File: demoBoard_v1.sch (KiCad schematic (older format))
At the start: 47 parts, among them P1 SPI_Header, P10 RTC_Serial, P11 WD_Header, P12 WD_1.2V_NC, P13 RTC_Aux, P14 Flash_3v3_NC, P15 WD_SENSE_3.3V_NC, P2 3x_CS_Header, P3 Power_Header, P4 LOAD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

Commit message: Fixed SEL monitor mistake ground connection
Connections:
- wire segments 172 -> 170
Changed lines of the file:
@@
 Text GLabel 4150 4800 2    60   Input ~ 0
 Load+
-Text GLabel 1250 3500 3    60   Input ~ 0
-INA_GND
 $Comp
 L DMN2075U Q1
@@
 Wire Wire Line
 	1000 7100 1000 7200
-Connection ~ 1100 3450
-Wire Wire Line
-	1250 3450 1100 3450
-Wire Wire Line
-	1250 3500 1250 3450
 Wire Wire Line
 	950  3400 900  3400
@@
 	1900 1100 1750 1100
 Wire Wire Line
-	9400 1100 9100 1100
+	9100 1100 9400 1100
 Wire Wire Line
 	9250 1100 9250 850

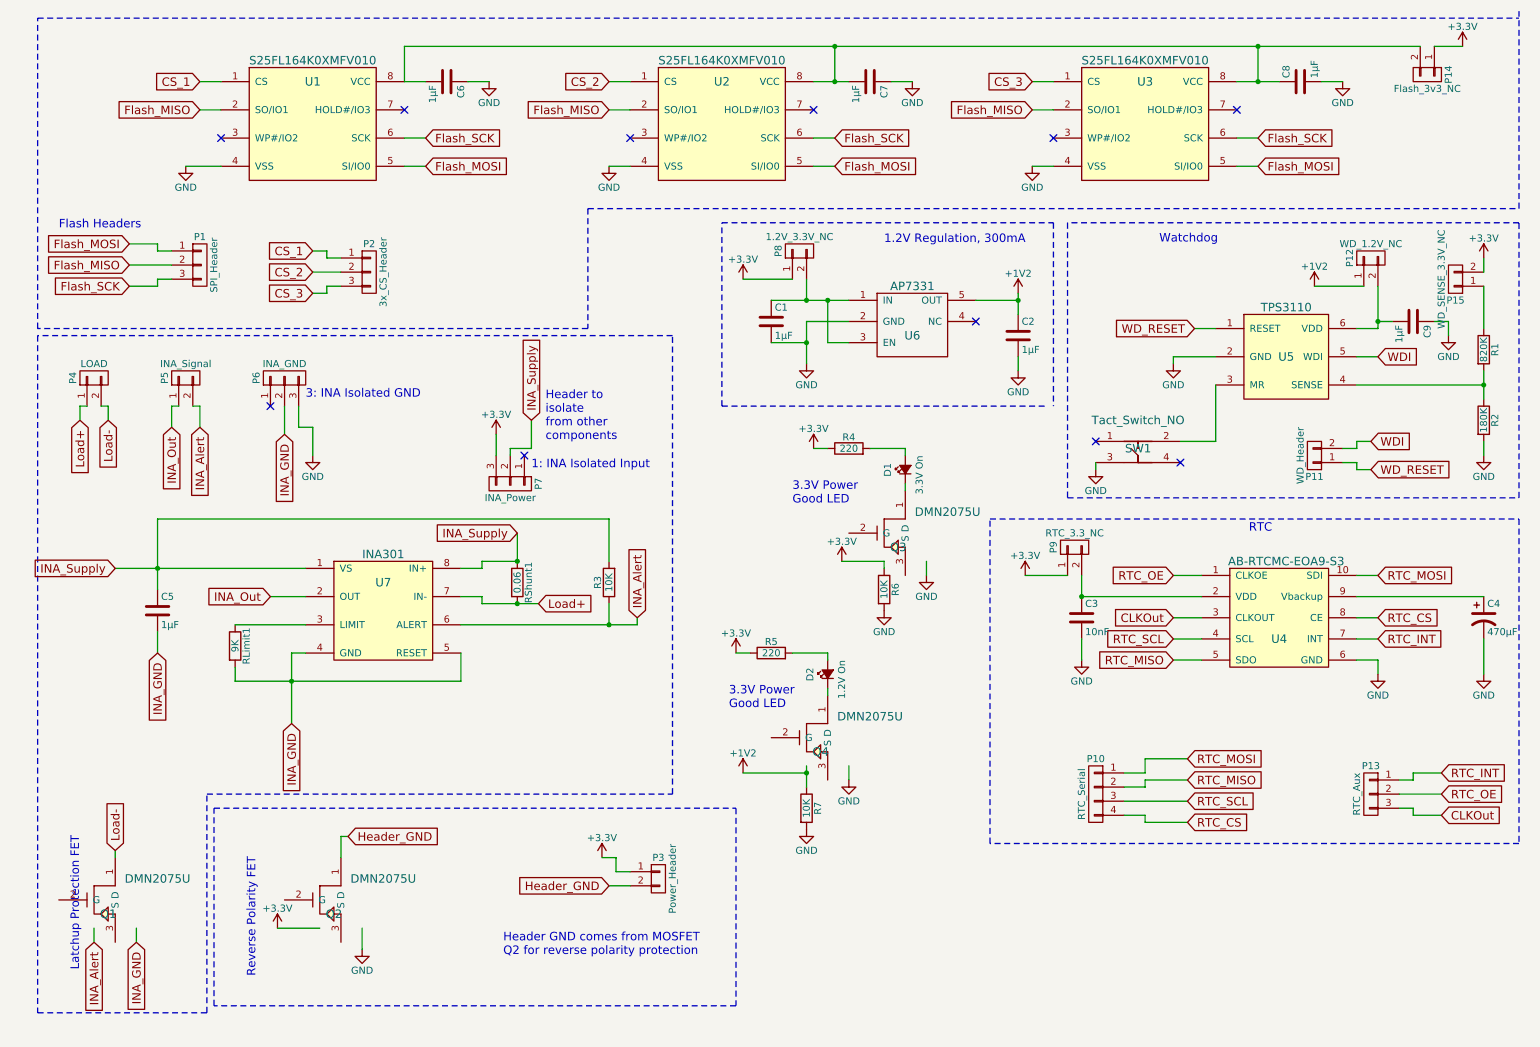
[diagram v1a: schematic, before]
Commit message: Added TVS and INA indicator LED to schematic. Committing before adding footprint and PCB traces.
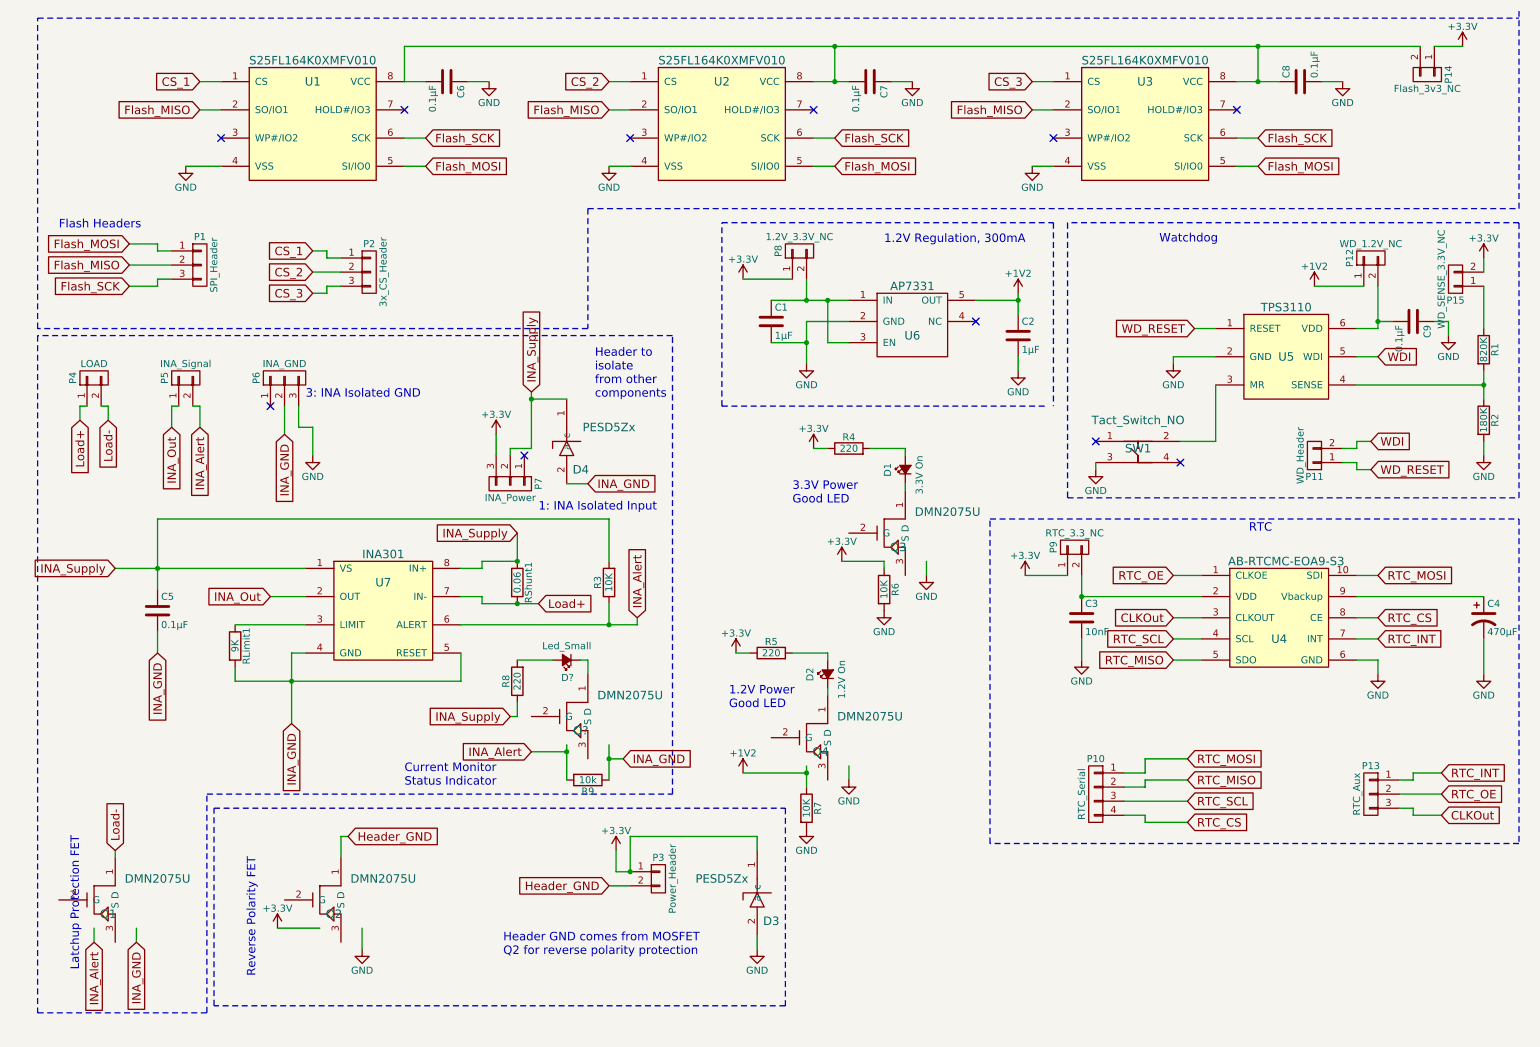
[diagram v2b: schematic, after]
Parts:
- added D3, D4: PESD5Zx, symbol PESD5Zx
- added D?: Led_Small, symbol Led_Small
- added Q?: DMN2075U, symbol DMN2075U
- added R8: 220, symbol R
- added R9: 10k, symbol R
- C5, C6, C7, C8, C9: value 1µF -> 0.1µF
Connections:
- wire segments 170 -> 184
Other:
- note added: "1.2V Power \nGood LED"
- note added: "Current Monitor\nStatus Indicator"

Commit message: Ready to be sent to board house
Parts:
- added R10: 0, Resistors_SMD:R_0402, symbol R
- D3, D4: footprint (none) -> SFUSat:PESD57zx
- D5: renamed from D?; footprint (none) -> SFUSat:LED_150060GS75000
- Q5: renamed from Q?; footprint (none) -> SFUSat:SOT23_DMN2075U
- R8, R9: footprint (none) -> Resistors_SMD:R_0402
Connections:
- wire segments 184 -> 185
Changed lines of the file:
@@
 F 0 "D3" H 5800 6650 60  0000 C CNN
 F 1 "PESD5Zx" H 5450 6950 60  0000 C CNN
-F 2 "" H 5700 6850 60  0001 C CNN
+F 2 "SFUSat:PESD57zx" H 5700 6850 60  0001 C CNN
 F 3 "" H 5700 6850 60  0001 C CNN
 	1    5700 6850
@@
 $EndComp
 $Comp
-L GND #PWR?
+L GND #PWR035
 U 1 1 5924F4C6
 P 5700 7250
-F 0 "#PWR?" H 5700 7000 50  0001 C CNN
+F 0 "#PWR035" H 5700 7000 50  0001 C CNN
 F 1 "GND" H 5700 7100 50  0000 C CNN
 F 2 "" H 5700 7250 50  0000 C CNN
@@
 F 0 "D4" H 4450 3450 60  0000 C CNN
 F 1 "PESD5Zx" H 4650 3750 60  0000 C CNN
-F 2 "" H 4350 3650 60  0001 C CNN
+F 2 "SFUSat:PESD57zx" H 4350 3650 60  0001 C CNN
 F 3 "" H 4350 3650 60  0001 C CNN
 	1    4350 3650
@@
 INA_GND
 $Comp
-L DMN2075U Q?
+L DMN2075U Q5
 U 1 1 592523F8
 P 4500 5600
-F 0 "Q?" H 4450 5500 60  0000 C CNN
+F 0 "Q5" H 4450 5500 60  0000 C CNN
 F 1 "DMN2075U" H 4800 5750 60  0000 C CNN
-F 2 "" H 4450 5500 60  0001 C CNN
+F 2 "SFUSat:SOT23_DMN2075U" H 4450 5500 60  0001 C CNN
 F 3 "" H 4450 5500 60  0001 C CNN
 	1    4500 5600
@@
 $EndComp
 $Comp
-L Led_Small D?
+L Led_Small D5
 U 1 1 59252552
 P 4350 5200
-F 0 "D?" H 4300 5325 50  0000 L CNN
+F 0 "D5" H 4300 5325 50  0000 L CNN
 F 1 "Led_Small" H 4175 5100 50  0000 L CNN
-F 2 "" V 4350 5200 50  0000 C CNN
+F 2 "SFUSat:LED_150060GS75000" V 4350 5200 50  0001 C CNN
 F 3 "" V 4350 5200 50  0000 C CNN
 	1    4350 5200
@@
 F 0 "R8" V 4080 5350 50  0000 C CNN
 F 1 "220" V 4000 5350 50  0000 C CNN
-F 2 "" V 3930 5350 50  0000 C CNN
+F 2 "Resistors_SMD:R_0402" V 3930 5350 50  0001 C CNN
 F 3 "" H 4000 5350 50  0000 C CNN
 	1    4000 5350
@@
 F 0 "R9" V 4580 6050 50  0000 C CNN
 F 1 "10k" V 4500 6050 50  0000 C CNN
-F 2 "" V 4430 6050 50  0000 C CNN
+F 2 "Resistors_SMD:R_0402" V 4430 6050 50  0001 C CNN
 F 3 "" H 4500 6050 50  0000 C CNN
 	1    4500 6050
@@
 	4350 5850 4100 5850
 Connection ~ 4350 5850
-Text GLabel 3950 5600 0    60   Input ~ 0
+Text GLabel 3450 5600 0    60   Input ~ 0
 INA_Supply
 Wire Wire Line
-	3950 5600 4000 5600
+	3850 5600 4000 5600
 Wire Wire Line
 	4000 5600 4000 5500
 Text Notes 3200 6100 0    60   ~ 0
 Current Monitor\nStatus Indicator
+$Comp
+L R R10
+U 1 1 5925159D
+P 3700 5600
+F 0 "R10" V 3780 5600 50  0000 C CNN
+F 1 "0" V 3700 5600 50  0000 C CNN
+F 2 "Resistors_SMD:R_0402" V 3630 5600 50  0001 C CNN
+F 3 "" H 3700 5600 50  0000 C CNN
+	1    3700 5600
+	0    1    1    0
+$EndComp
+Wire Wire Line
+	3550 5600 3450 5600
 $EndSCHEMATC

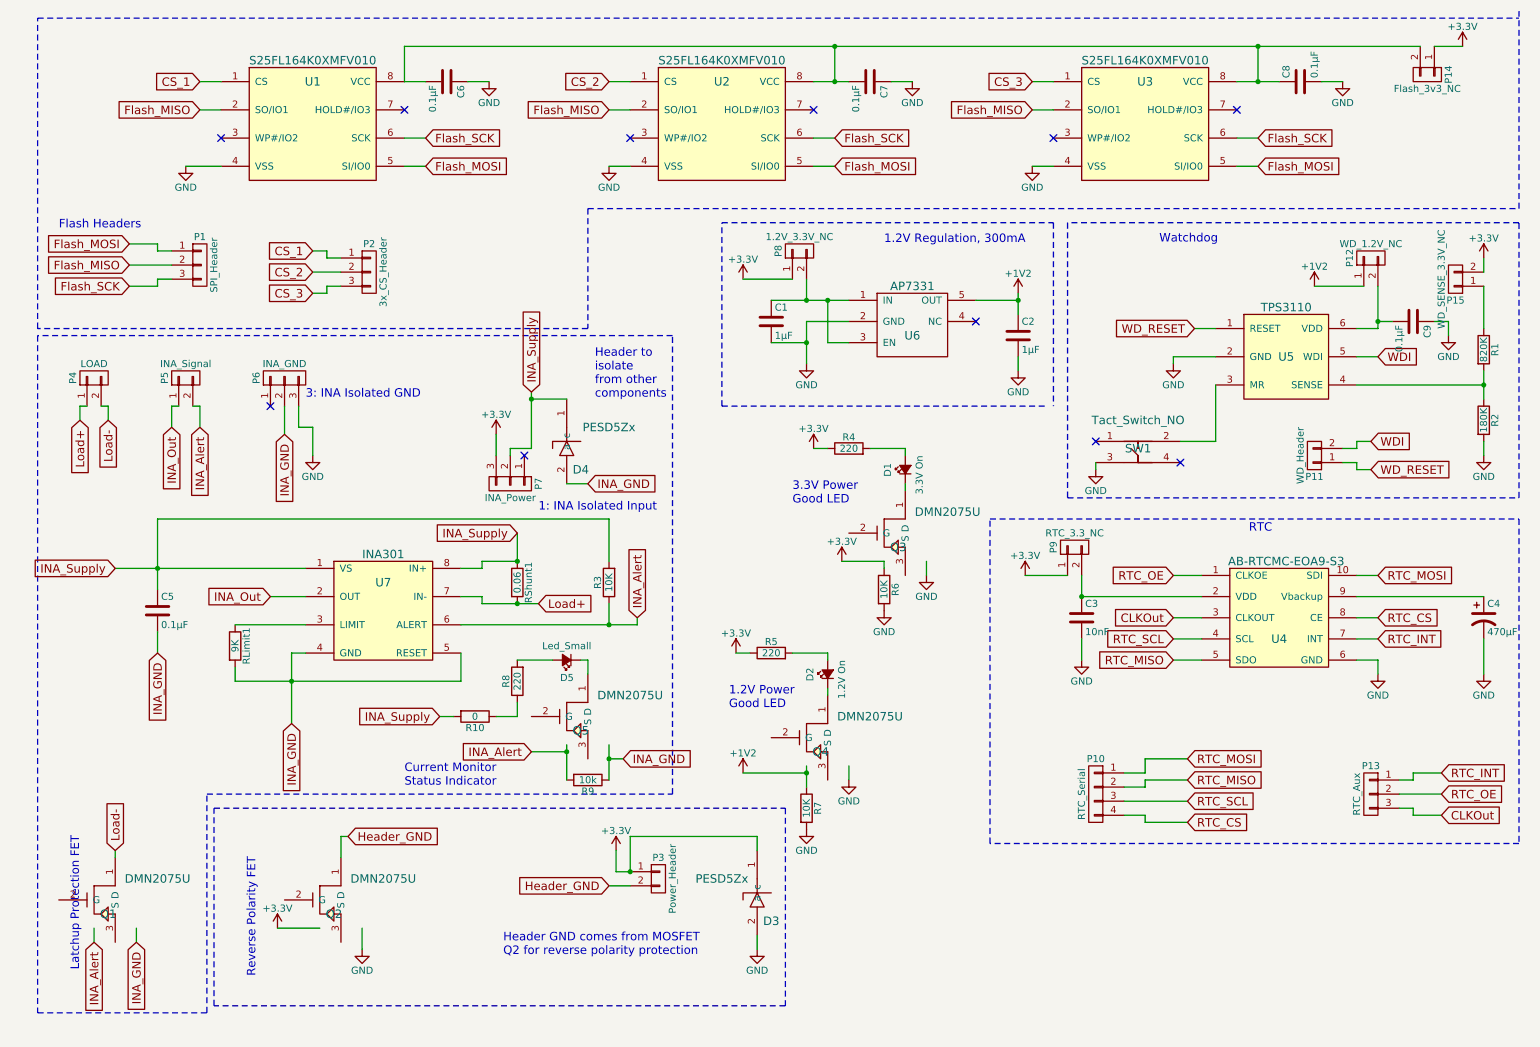
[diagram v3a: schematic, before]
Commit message: Updated LED resistors to 30 ohm, turned RLimit1 into RLimit1 and RLimit2 which are values you can actually buy. Made pin header holes slightly bigger, regenerated gerbers
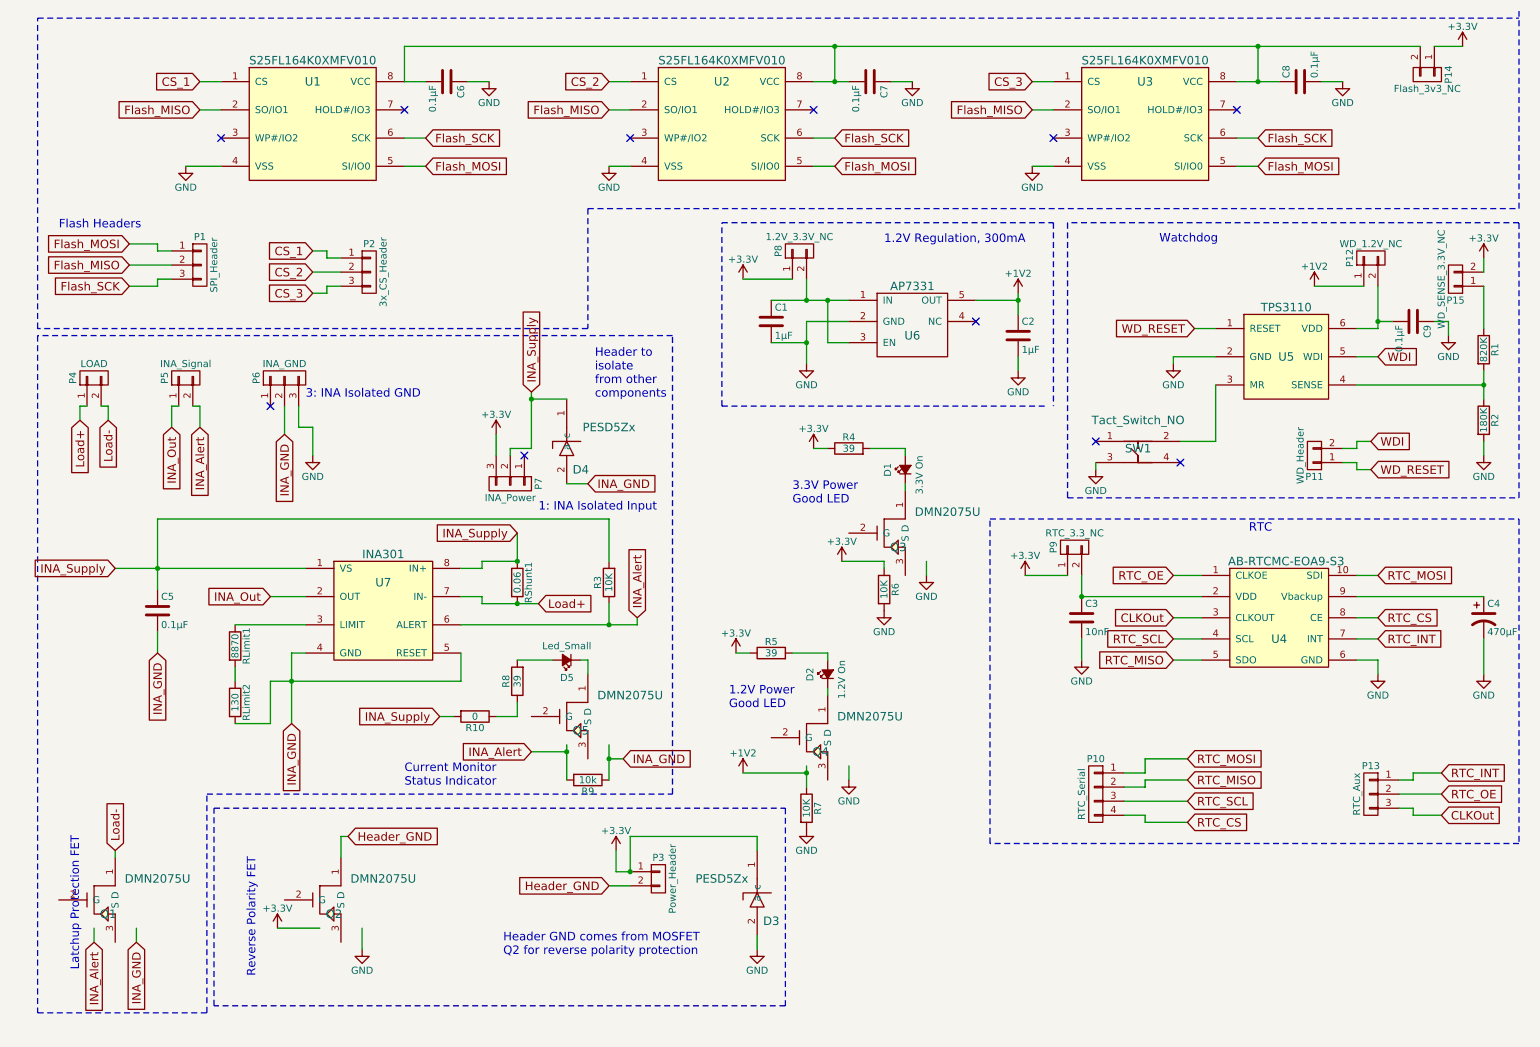
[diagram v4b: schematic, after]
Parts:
- added RLimit2: 130, Resistors_SMD:R_0402, symbol R
- R4, R5, R8: value 220 -> 39
- RLimit1: value 9K -> 8870
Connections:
- wire segments 185 -> 187
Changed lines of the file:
@@
 P 2000 5100
 F 0 "RLimit1" V 2080 5100 50  0000 C CNN
-F 1 "9K" V 2000 5100 50  0000 C CNN
+F 1 "8870" V 2000 5100 50  0000 C CNN
 F 2 "Resistors_SMD:R_0402" V 1930 5100 50  0001 C CNN
 F 3 "" H 2000 5100 50  0000 C CNN
@@
 P 6350 3700
 F 0 "R4" V 6430 3700 50  0000 C CNN
-F 1 "220" V 6350 3700 50  0000 C CNN
+F 1 "39" V 6350 3700 50  0000 C CNN
 F 2 "Resistors_SMD:R_0402" V 6280 3700 50  0001 C CNN
 F 3 "" H 6350 3700 50  0000 C CNN
@@
 P 5800 5150
 F 0 "R5" V 5880 5150 50  0000 C CNN
-F 1 "220" V 5800 5150 50  0000 C CNN
+F 1 "39" V 5800 5150 50  0000 C CNN
 F 2 "Resistors_SMD:R_0402" V 5730 5150 50  0001 C CNN
 F 3 "" H 5800 5150 50  0000 C CNN
@@
 P 4000 5350
 F 0 "R8" V 4080 5350 50  0000 C CNN
-F 1 "220" V 4000 5350 50  0000 C CNN
+F 1 "39" V 4000 5350 50  0000 C CNN
 F 2 "Resistors_SMD:R_0402" V 3930 5350 50  0001 C CNN
 F 3 "" H 4000 5350 50  0000 C CNN
@@
 Connection ~ 9250 850
 Wire Wire Line
-	9250 1100 9250 850
+	9250 850  9250 1100
 Wire Wire Line
 	9100 1100 9400 1100
@@
 	5450 3400 7750 3400
 Wire Wire Line
-	2000 5350 3600 5350
+	2250 5350 3600 5350
 Connection ~ 2400 5350
 Wire Wire Line
@@
 Connection ~ 4650 5900
 Wire Wire Line
-	4350 6050 4350 5800
+	4350 5800 4350 6050
 Wire Wire Line
 	4350 5850 4100 5850
@@
 Wire Wire Line
 	3550 5600 3450 5600
+$Comp
+L R RLimit2
+U 1 1 592670AC
+P 2000 5500
+F 0 "RLimit2" V 2080 5500 50  0000 C CNN
+F 1 "130" V 2000 5500 50  0000 C CNN
+F 2 "Resistors_SMD:R_0402" V 1930 5500 50  0001 C CNN
+F 3 "" H 2000 5500 50  0000 C CNN
+	1    2000 5500
+	1    0    0    -1
+$EndComp
+Wire Wire Line
+	2000 5650 2250 5650
+Wire Wire Line
+	2250 5650 2250 5350
 $EndSCHEMATC
